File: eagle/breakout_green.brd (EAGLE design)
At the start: 28.6 x 28.6 mm, 19 parts, among them X1 734120110

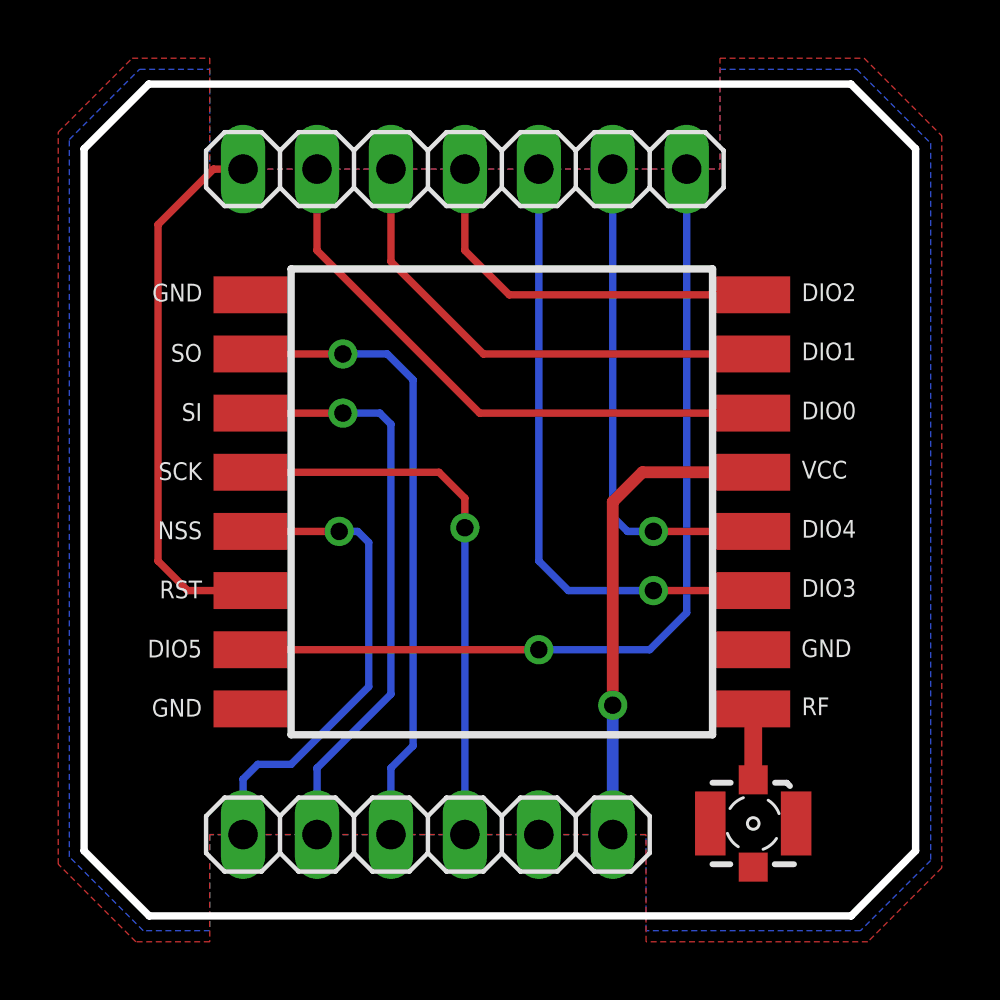
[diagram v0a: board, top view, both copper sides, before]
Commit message: Fixed LoRa module pad spacing
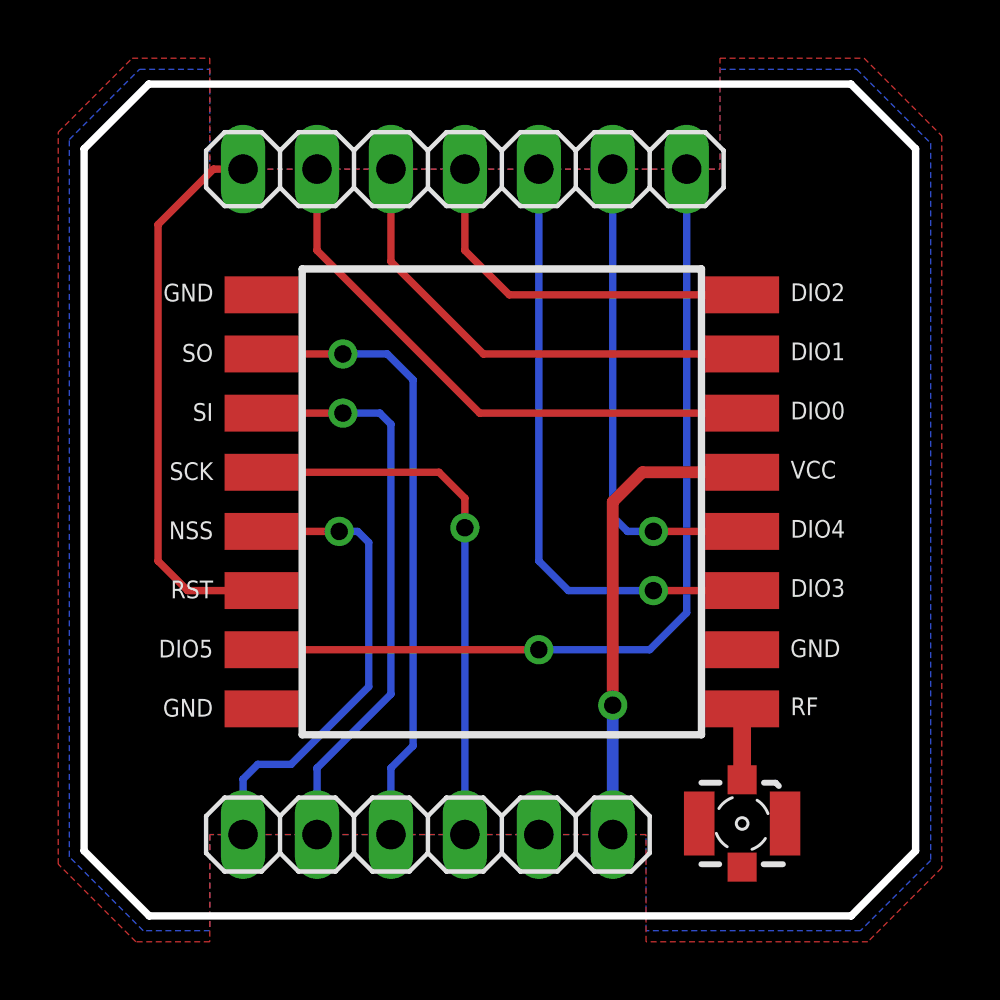
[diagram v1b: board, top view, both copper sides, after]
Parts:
- moved DIO5 0.38 mm to (6.10, 9.14)
- moved GND 0.38 mm to (6.10, 7.11)
- moved GND2 0.38 mm to (6.10, 21.3)
- moved NSS 0.38 mm to (6.10, 13.2)
- moved RST 0.38 mm to (6.10, 11.2)
- moved SCK 0.38 mm to (6.10, 15.2)
- moved SI 0.38 mm to (6.10, 17.3)
- moved SO 0.38 mm to (6.10, 19.3)
- moved DIO0 0.38 mm to (22.6, 17.3)
- moved DIO1 0.38 mm to (22.6, 19.3)
- moved DIO2 0.38 mm to (22.6, 21.3)
- moved DIO3 0.38 mm to (22.6, 11.2)
- moved DIO4 0.38 mm to (22.6, 13.2)
- moved GND_RF 0.38 mm to (22.6, 9.14)
- moved RF 0.38 mm to (22.6, 7.11)
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
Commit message: Shield and breakout layout update
Added a gap to the pin headers on LoRa breakout board and the shield to enforce breakout orientation.
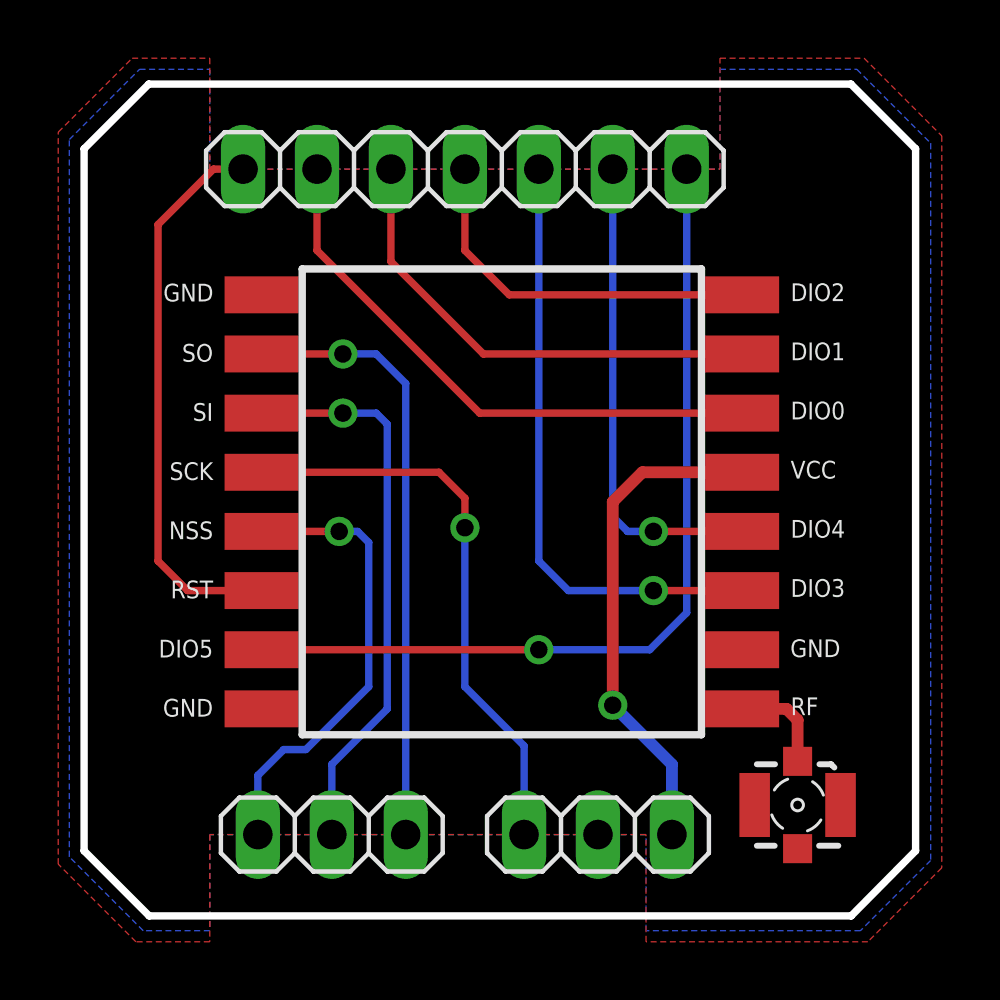
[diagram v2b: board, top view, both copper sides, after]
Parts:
- removed JP2: (no value), pinhead:1X06
- added JP2A, JP2B: (no value), pinhead:1X03
- moved X1 2.01 mm to (24.5, 3.81)
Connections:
- net 3.3V: now also JP2A.1; no longer JP2.1
- net GND: now also JP2A.2; no longer JP2.2
- net MISO: now also JP2B.1; no longer JP2.4
- net MOSI: now also JP2B.2; no longer JP2.5
- net NSS: now also JP2B.3; no longer JP2.6
- net SCK: now also JP2A.3; no longer JP2.3
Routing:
- net ANT: track 2.44 -> 3.48 mm
- net 3.3V: track 16.3 -> 17.1 mm
- net SCK: track 18.9 -> 19.8 mm
- net MISO: track 21.5 -> 20.9 mm
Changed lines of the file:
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@@
 <attribute name="VALUE" x="4.191" y="22.479" size="1.27" layer="27"/>
-</element>
-<element name="JP2" library="pinhead" package="1X06" value="" x="11.811" y="2.794" smashed="yes" rot="R180">
-<attribute name="VALUE" x="19.431" y="5.969" size="1.27" layer="27" rot="R180"/>
 </element>
 <element name="RST" library="wirepad" package="SMD1,27-2,54" value="" x="6.096" y="11.176" smashed="yes" rot="R90">
@@
 <attribute name="NAME" x="4.432" y="13.551" size="0.6096" layer="25" rot="R180"/>
 </element>
-<element name="X1" library="con-coax" package="734120110" value="734120110" x="22.606" y="3.175" smashed="yes" rot="R180"/>
+<element name="X1" library="con-coax" package="734120110" value="734120110" x="24.511" y="3.81" smashed="yes" rot="R180"/>
 <element name="GND2" library="wirepad" package="SMD1,27-2,54" value="" x="6.096" y="21.336" smashed="yes" rot="R270"/>
+<element name="JP2A" library="pinhead" package="1X03" value="" x="17.653" y="2.794" smashed="yes" rot="R180">
+<attribute name="VALUE" x="21.463" y="5.969" size="1.27" layer="27" rot="R180"/>
+</element>
+<element name="JP2B" library="pinhead" package="1X03" value="" x="8.509" y="2.794" smashed="yes" rot="R180">
+<attribute name="VALUE" x="12.319" y="5.969" size="1.27" layer="27" rot="R180"/>
+</element>
 </elements>
 <signals>
@@
 <signal name="3.3V">
 <contactref element="VCC" pad="1"/>
-<contactref element="JP2" pad="1"/>
 <wire x1="18.161" y1="7.239" x2="18.161" y2="14.224" width="0.4064" layer="1"/>
 <wire x1="18.161" y1="14.224" x2="19.177" y2="15.24" width="0.4064" layer="1"/>
 <wire x1="19.177" y1="15.24" x2="22.606" y2="15.24" width="0.4064" layer="1"/>
 <via x="18.161" y="7.239" extent="1-16" drill="0.6"/>
-<wire x1="18.161" y1="7.239" x2="18.161" y2="2.794" width="0.4064" layer="16"/>
+<contactref element="JP2A" pad="1"/>
+<wire x1="18.161" y1="7.239" x2="20.193" y2="5.207" width="0.4064" layer="16"/>
+<wire x1="20.193" y1="5.207" x2="20.193" y2="2.794" width="0.4064" layer="16"/>
 </signal>
 <signal name="SCK">
 <contactref element="SCK" pad="1"/>
-<contactref element="JP2" pad="3"/>
-<wire x1="13.081" y1="2.794" x2="13.081" y2="13.335" width="0.254" layer="16"/>
 <via x="13.081" y="13.335" extent="1-16" drill="0.6"/>
 <wire x1="13.081" y1="13.335" x2="13.081" y2="14.351" width="0.254" layer="1"/>
 <wire x1="13.081" y1="14.351" x2="12.192" y2="15.24" width="0.254" layer="1"/>
 <wire x1="12.192" y1="15.24" x2="6.096" y2="15.24" width="0.254" layer="1"/>
+<contactref element="JP2A" pad="3"/>
+<wire x1="13.081" y1="13.335" x2="13.081" y2="7.874" width="0.254" layer="16"/>
+<wire x1="13.081" y1="7.874" x2="15.113" y2="5.842" width="0.254" layer="16"/>
+<wire x1="15.113" y1="5.842" x2="15.113" y2="2.794" width="0.254" layer="16"/>
 </signal>
 <signal name="MISO">
 <contactref element="SO" pad="1"/>
-<contactref element="JP2" pad="4"/>
-<wire x1="10.541" y1="2.794" x2="10.541" y2="5.08" width="0.254" layer="16"/>
-<wire x1="10.541" y1="5.08" x2="11.303" y2="5.842" width="0.254" layer="16"/>
-<wire x1="11.303" y1="5.842" x2="11.303" y2="18.415" width="0.254" layer="16"/>
-<wire x1="11.303" y1="18.415" x2="10.414" y2="19.304" width="0.254" layer="16"/>
-<wire x1="10.414" y1="19.304" x2="8.89" y2="19.304" width="0.254" layer="16"/>
+<wire x1="11.049" y1="2.794" x2="11.049" y2="18.288" width="0.254" layer="16"/>
+<wire x1="11.049" y1="18.288" x2="10.033" y2="19.304" width="0.254" layer="16"/>
+<wire x1="10.033" y1="19.304" x2="8.89" y2="19.304" width="0.254" layer="16"/>
 <via x="8.89" y="19.304" extent="1-16" drill="0.6"/>
 <wire x1="8.89" y1="19.304" x2="6.096" y2="19.304" width="0.254" layer="1"/>
+<contactref element="JP2B" pad="1"/>
 </signal>
 <signal name="MOSI">
 <contactref element="SI" pad="1"/>
-<contactref element="JP2" pad="5"/>
 <wire x1="6.096" y1="17.272" x2="8.89" y2="17.272" width="0.254" layer="1"/>
 <via x="8.89" y="17.272" extent="1-16" drill="0.6"/>
-<wire x1="8.89" y1="17.272" x2="10.16" y2="17.272" width="0.254" layer="16"/>
-<wire x1="10.16" y1="17.272" x2="10.541" y2="16.891" width="0.254" layer="16"/>
-<wire x1="10.541" y1="16.891" x2="10.541" y2="7.62" width="0.254" layer="16"/>
-<wire x1="10.541" y1="7.62" x2="8.001" y2="5.08" width="0.254" layer="16"/>
-<wire x1="8.001" y1="5.08" x2="8.001" y2="2.794" width="0.254" layer="16"/>
+<wire x1="8.89" y1="17.272" x2="10.033" y2="17.272" width="0.254" layer="16"/>
+<wire x1="10.033" y1="17.272" x2="10.414" y2="16.891" width="0.254" layer="16"/>
+<wire x1="10.414" y1="16.891" x2="10.414" y2="7.112" width="0.254" layer="16"/>
+<wire x1="10.414" y1="7.112" x2="8.509" y2="5.207" width="0.254" layer="16"/>
+<contactref element="JP2B" pad="2"/>
+<wire x1="8.509" y1="5.207" x2="8.509" y2="2.794" width="0.254" layer="16"/>
 </signal>
 <signal name="NSS">
 <contactref element="NSS" pad="1"/>
-<contactref element="JP2" pad="6"/>
 <wire x1="6.096" y1="13.208" x2="8.763" y2="13.208" width="0.254" layer="1"/>
 <via x="8.763" y="13.208" extent="1-16" drill="0.6"/>
@@
 <wire x1="9.398" y1="13.208" x2="9.779" y2="12.827" width="0.254" layer="16"/>
 <wire x1="9.779" y1="12.827" x2="9.779" y2="7.874" width="0.254" layer="16"/>
-<wire x1="9.779" y1="7.874" x2="7.112" y2="5.207" width="0.254" layer="16"/>
-<wire x1="7.112" y1="5.207" x2="5.969" y2="5.207" width="0.254" layer="16"/>
-<wire x1="5.969" y1="5.207" x2="5.461" y2="4.699" width="0.254" layer="16"/>
-<wire x1="5.461" y1="4.699" x2="5.461" y2="2.794" width="0.254" layer="16"/>
+<wire x1="9.779" y1="7.874" x2="7.62" y2="5.715" width="0.254" layer="16"/>
+<wire x1="7.62" y1="5.715" x2="6.858" y2="5.715" width="0.254" layer="16"/>
+<wire x1="6.858" y1="5.715" x2="5.969" y2="4.826" width="0.254" layer="16"/>
+<contactref element="JP2B" pad="3"/>
+<wire x1="5.969" y1="4.826" x2="5.969" y2="2.794" width="0.254" layer="16"/>
 </signal>
 <signal name="ANT">
 <contactref element="RF" pad="1"/>
 <contactref element="X1" pad="1"/>
-<wire x1="22.606" y1="7.112" x2="22.606" y2="4.675" width="0.6096" layer="1"/>
+<wire x1="22.606" y1="7.112" x2="24.13" y2="7.112" width="0.4064" layer="1"/>
+<wire x1="24.13" y1="7.112" x2="24.511" y2="6.731" width="0.4064" layer="1"/>
+<wire x1="24.511" y1="6.731" x2="24.511" y2="5.31" width="0.4064" layer="1"/>
 </signal>
 <signal name="GND">
 <contactref element="GND" pad="1"/>
-<contactref element="JP2" pad="2"/>
 <polygon width="0.4064" layer="1">
 <vertex x="1.651" y="29.464"/>
@@
 <contactref element="X1" pad="S@2"/>
 <contactref element="X1" pad="S@3"/>
+<contactref element="JP2A" pad="2"/>
 </signal>
 <signal name="DIO2">
